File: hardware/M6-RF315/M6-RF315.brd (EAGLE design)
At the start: 90 x 56 mm, 42 parts, among them J1 CON-71439-2164, J2 CON-SMA-VERT, M1 MOUNT-HOLE3.3, M2 MOUNT-HOLE3.3, M3 MOUNT-HOLE3.3, M4 MOUNT-HOLE3.3, M5 FIDUCIAL1X2, M6 FIDUCIAL1X2, M7 FIDUCIAL1X2, M8 FIDUCIAL1X2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

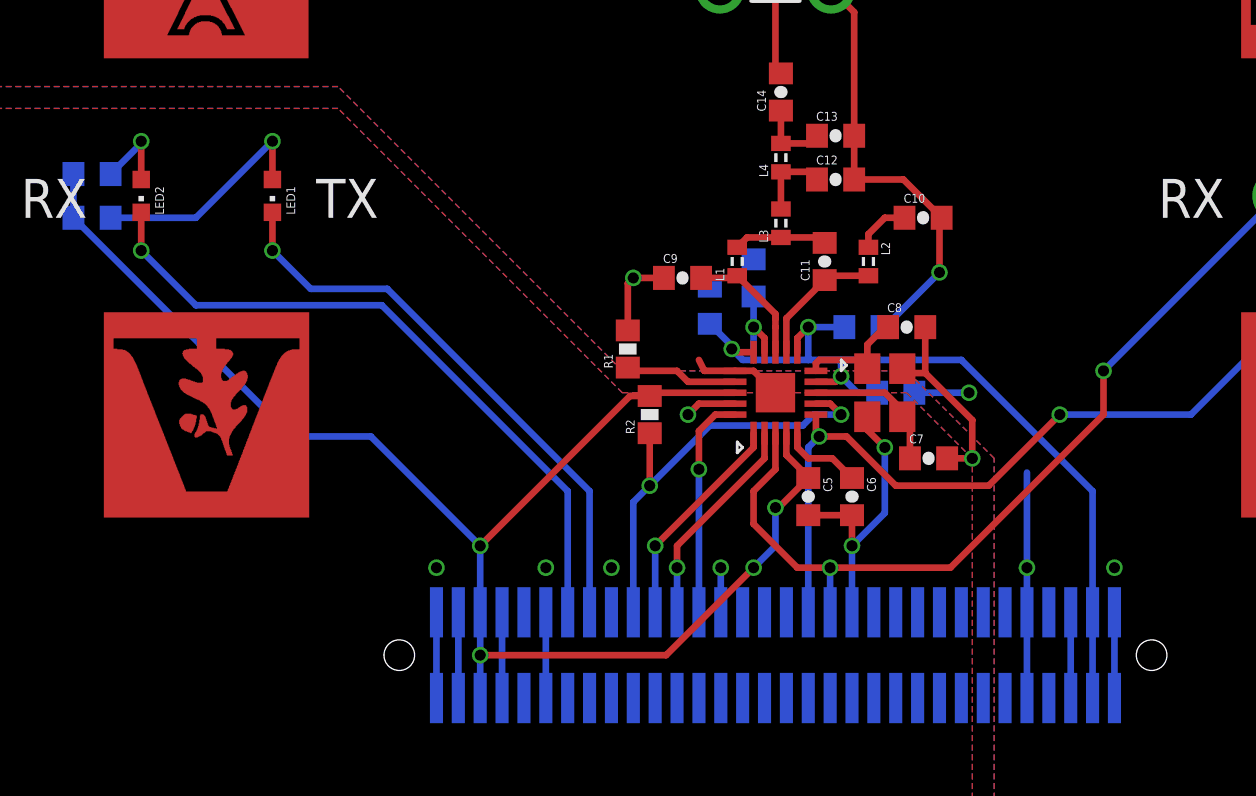
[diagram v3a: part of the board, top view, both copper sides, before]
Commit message: Updated BOM and removed some DRC errors.
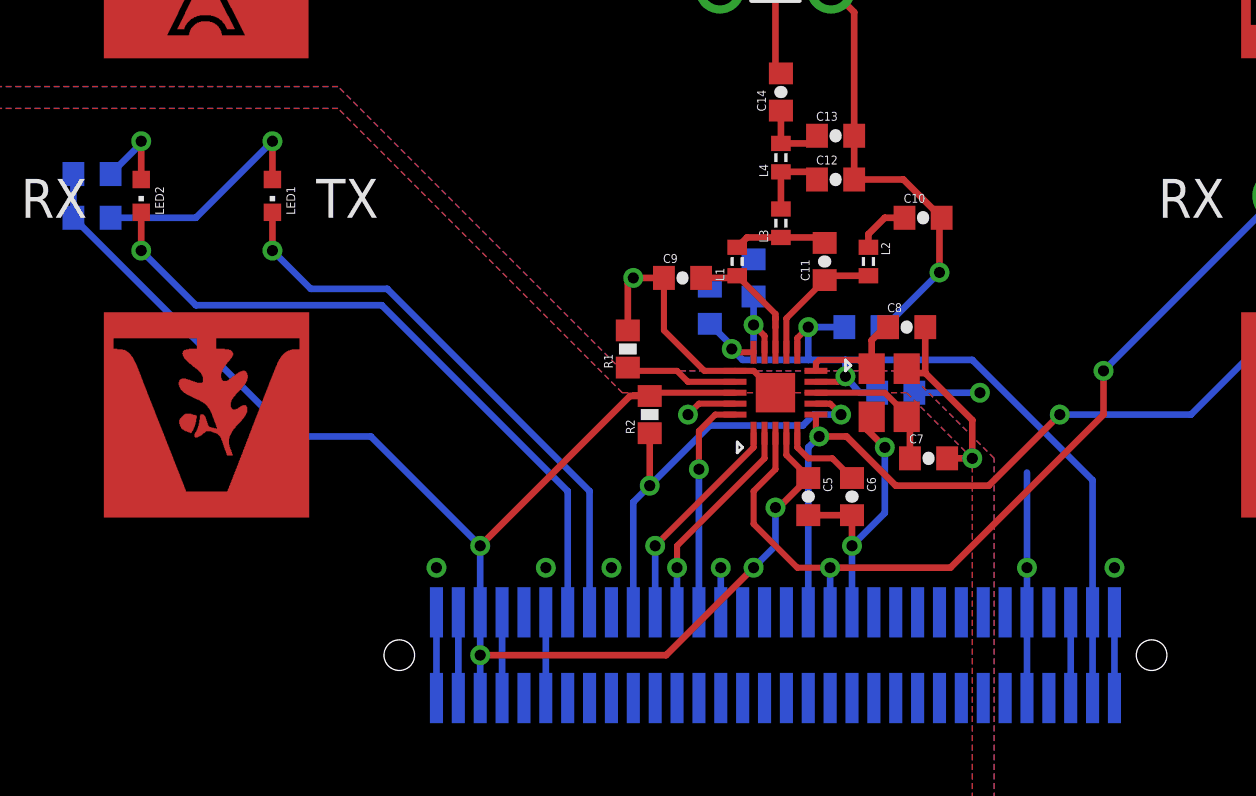
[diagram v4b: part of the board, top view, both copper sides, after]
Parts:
- moved X1 0.20 mm to (50.2, 19.0)
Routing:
- net AGND: track 60.5 -> 65.5 mm

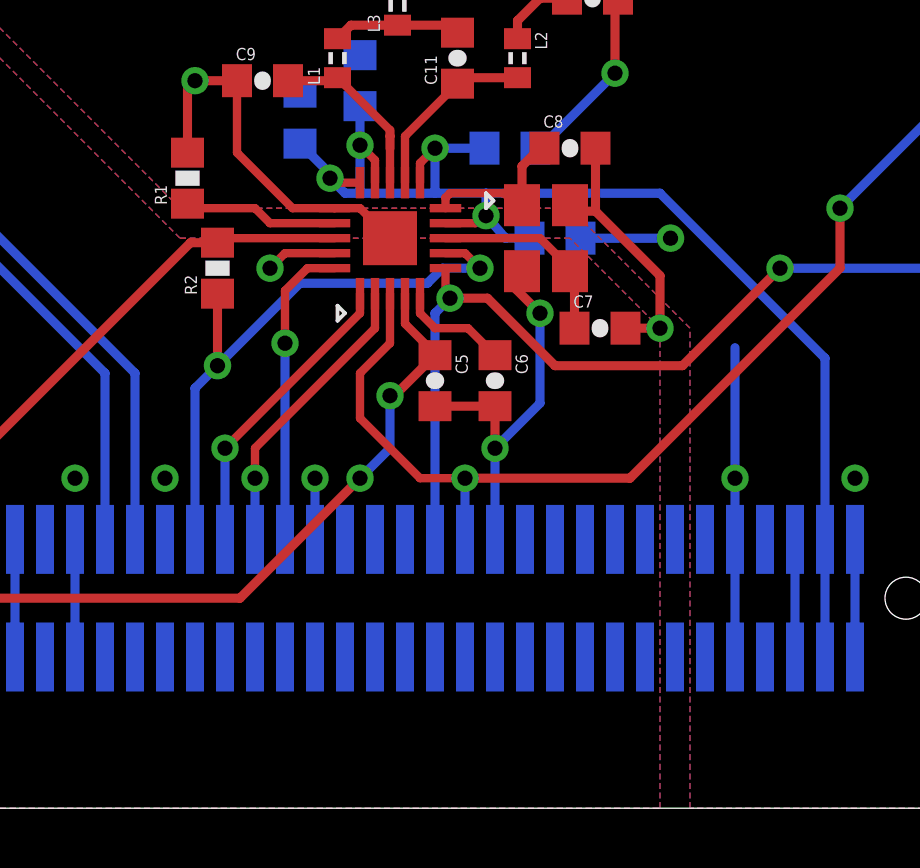
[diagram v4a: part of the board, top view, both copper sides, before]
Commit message: Reviewed DRC errors.
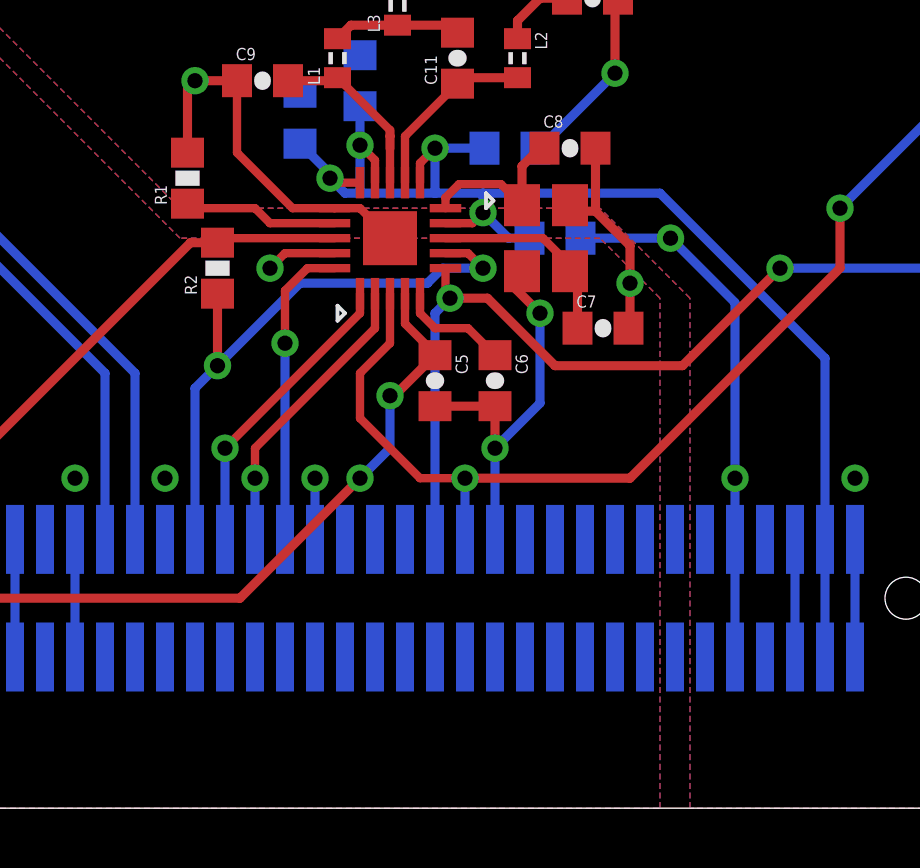
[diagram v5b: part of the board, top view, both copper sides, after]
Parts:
- moved C7 0.10 mm to (52.1, 16.0)
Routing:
- net AGND: track 65.5 -> 70.0 mm
- net DGND: track 34.7 -> 33.1 mm
- net N$7: track 6.94 -> 7.45 mm
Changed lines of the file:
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@@
 <setting verticaltext="up"/>
 </settings>
-<grid distance="1" unitdist="mm" unit="mm" style="lines" multiple="1" display="yes" altdistance="0.1" altunitdist="mm" altunit="mm"/>
+<grid distance="1" unitdist="mm" unit="mm" style="lines" multiple="1" display="yes" altdistance="0.5" altunitdist="mm" altunit="mm"/>
 <layers>
 <layer number="1" name="Top" color="4" fill="1" visible="yes" active="yes"/>
@@
 </element>
 <element name="C6" library="M6-RF315" package="C0603" value="100nF" x="48.5" y="14.25" rot="R270"/>
-<element name="C7" library="M6-RF315" package="C0603" value="12pF" x="52" y="16"/>
+<element name="C7" library="M6-RF315" package="C0603" value="12pF" x="52.1" y="16"/>
 <element name="C8" library="M6-RF315" package="C0603" value="15pF" x="51" y="22"/>
 <element name="TP1" library="M6-RF315" package="TESTPOINT" value="TESTPOINT-RED" x="74" y="28">
@@
 <vertex x="0" y="0"/>
 <vertex x="54" y="0"/>
-<vertex x="54" y="16"/>
-<vertex x="51" y="19"/>
+<vertex x="54" y="17"/>
+<vertex x="52" y="19"/>
 <vertex x="38" y="19"/>
 <vertex x="25" y="32"/>
@@
 <vertex x="0" y="0"/>
 <vertex x="54" y="0"/>
-<vertex x="54" y="16"/>
-<vertex x="51" y="19"/>
+<vertex x="54" y="17"/>
+<vertex x="52" y="19"/>
 <vertex x="38" y="19"/>
 <vertex x="25" y="32"/>
@@
 <wire x1="49.4" y1="17.9" x2="49.2" y2="17.3" width="0.3048" layer="1"/>
 <wire x1="49.2" y1="17.3" x2="50" y2="16.5" width="0.3048" layer="1"/>
-<via x="54" y="16" extent="1-16" drill="0.508"/>
-<wire x1="52.85" y1="16" x2="54" y2="16" width="0.3048" layer="1"/>
+<via x="53" y="17.5" extent="1-16" drill="0.508"/>
 <wire x1="51.85" y1="22" x2="51.85" y2="19.9" width="0.3048" layer="1"/>
-<wire x1="51.85" y1="19.9" x2="54" y2="17.75" width="0.3048" layer="1"/>
-<wire x1="54" y1="17.75" x2="54" y2="16" width="0.3048" layer="1"/>
+<wire x1="51.85" y1="19.9" x2="53" y2="18.75" width="0.3048" layer="1"/>
 <wire x1="51" y1="20.1" x2="51" y2="19.9" width="0.3048" layer="1"/>
 <wire x1="51" y1="19.9" x2="51.85" y2="19.9" width="0.3048" layer="1"/>
@@
 <wire x1="42.5" y1="8.96" x2="42.5" y2="11" width="0.3048" layer="16"/>
 <wire x1="41.5" y1="18.5" x2="41" y2="18" width="0.2794" layer="1"/>
+<wire x1="53" y1="18.75" x2="53" y2="17.5" width="0.3048" layer="1"/>
+<wire x1="53" y1="17.5" x2="53" y2="16.05" width="0.3048" layer="1"/>
+<wire x1="53" y1="16.05" x2="52.95" y2="16" width="0.3048" layer="1"/>
 </signal>
 <signal name="VSUP">
@@
 <wire x1="46" y1="21.5" x2="46.5" y2="22" width="0.2794" layer="1"/>
 <via x="46.5" y="22" extent="1-16" drill="0.508"/>
-<wire x1="46.85" y1="19.5" x2="47.85" y2="19.5" width="0.2794" layer="1"/>
-<wire x1="47.85" y1="19.5" x2="48.2" y2="19.75" width="0.2794" layer="1"/>
-<via x="48.2" y="19.75" extent="1-16" drill="0.508"/>
+<wire x1="46.85" y1="19.5" x2="47.75" y2="19.5" width="0.2794" layer="1"/>
+<wire x1="47.75" y1="19.5" x2="48.1" y2="19.85" width="0.2794" layer="1"/>
+<via x="48.1" y="19.85" extent="1-16" drill="0.508"/>
 <wire x1="44.5" y1="20.85" x2="44.5" y2="21.6" width="0.2794" layer="1"/>
 <via x="44" y="22.1" extent="1-16" drill="0.508"/>
@@
 <wire x1="59.5" y1="8.96" x2="59.5" y2="15" width="0.3048" layer="16"/>
 <wire x1="59.5" y1="15" x2="54" y2="20.5" width="0.3048" layer="16"/>
-<wire x1="54" y1="20.5" x2="48.2" y2="20.5" width="0.3048" layer="16"/>
-<wire x1="48.2" y1="20.5" x2="46.5" y2="20.5" width="0.3048" layer="16"/>
+<wire x1="54" y1="20.5" x2="48.1" y2="20.5" width="0.3048" layer="16"/>
+<wire x1="48.1" y1="20.5" x2="46.5" y2="20.5" width="0.3048" layer="16"/>
 <wire x1="46.5" y1="22" x2="46.5" y2="20.5" width="0.3048" layer="16"/>
-<wire x1="48.2" y1="19.75" x2="48.2" y2="20.5" width="0.3048" layer="16"/>
+<wire x1="48.1" y1="19.85" x2="48.1" y2="20.5" width="0.3048" layer="16"/>
 <via x="43" y="21" extent="1-16" drill="0.508"/>
 <wire x1="42" y1="22.15" x2="43" y2="21.15" width="0.3048" layer="16"/>
@@
 <wire x1="43.5" y1="20.5" x2="44" y2="20.5" width="0.3048" layer="16"/>
 <wire x1="44" y1="20.5" x2="46.5" y2="20.5" width="0.3048" layer="16"/>
-<wire x1="49.65" y1="19" x2="48.85" y2="19" width="0.3048" layer="16"/>
-<wire x1="48.85" y1="19" x2="48.2" y2="19.75" width="0.3048" layer="16"/>
+<wire x1="49.65" y1="19" x2="48.95" y2="19" width="0.3048" layer="16"/>
+<wire x1="48.95" y1="19" x2="48.1" y2="19.85" width="0.3048" layer="16"/>
 <wire x1="46.5" y1="22" x2="48.15" y2="22" width="0.3048" layer="16"/>
 <wire x1="44" y1="20.85" x2="43.15" y2="20.85" width="0.2794" layer="1"/>
@@
 <contactref element="U1" pad="7"/>
 <contactref element="R2" pad="1"/>
-<wire x1="46.85" y1="18.5" x2="47.5" y2="18.5" width="0.2794" layer="1"/>
-<wire x1="47.5" y1="18.5" x2="48" y2="18" width="0.2794" layer="1"/>
-<via x="48" y="18" extent="1-16" drill="0.508"/>
-<wire x1="48" y1="18" x2="46.75" y2="18" width="0.3048" layer="16"/>
+<wire x1="46.85" y1="18.5" x2="47.6" y2="18.5" width="0.2794" layer="1"/>
+<wire x1="47.6" y1="18.5" x2="48.1" y2="18" width="0.2794" layer="1"/>
+<via x="48.1" y="18" extent="1-16" drill="0.508"/>
+<wire x1="48.1" y1="18" x2="46.75" y2="18" width="0.3048" layer="16"/>
 <wire x1="46.75" y1="18" x2="46.25" y2="17.5" width="0.3048" layer="16"/>
 <wire x1="46.25" y1="17.5" x2="42" y2="17.5" width="0.3048" layer="16"/>
@@
 <vertex x="90" y="0"/>
 <vertex x="55" y="0"/>
-<vertex x="55" y="16"/>
-<vertex x="51" y="20"/>
+<vertex x="55" y="17"/>
+<vertex x="52" y="20"/>
 <vertex x="38" y="20"/>
 <vertex x="25" y="33"/>
@@
 <vertex x="90" y="0"/>
 <vertex x="55" y="0"/>
-<vertex x="55" y="16"/>
-<vertex x="51" y="20"/>
+<vertex x="55" y="17"/>
+<vertex x="52" y="20"/>
 <vertex x="38" y="20"/>
 <vertex x="25" y="33"/>
@@
 <wire x1="60.5" y1="8.96" x2="60.5" y2="5.04" width="0.3048" layer="16"/>
 <wire x1="56.5" y1="8.96" x2="56.5" y2="11" width="0.3048" layer="16"/>
-<wire x1="56.5" y1="11" x2="56.5" y2="15.35" width="0.3048" layer="16"/>
+<wire x1="56.5" y1="11" x2="56.5" y2="16.85" width="0.3048" layer="16"/>
 <via x="38.5" y="24.25" extent="1-16" drill="0.508"/>
 <wire x1="43.15" y1="20" x2="41.75" y2="20" width="0.2794" layer="1"/>
@@
 <wire x1="41.75" y1="20" x2="39.9" y2="21.85" width="0.2794" layer="1"/>
 <wire x1="39.9" y1="21.85" x2="39.9" y2="24.25" width="0.2794" layer="1"/>
-<wire x1="60.5" y1="8.96" x2="60.5" y2="11" width="0" layer="19" extent="16-16"/>
-<wire x1="56.5" y1="11" x2="60.5" y2="11" width="0" layer="19" extent="16-16"/>
-<wire x1="54.35" y1="19" x2="56.5" y2="15.35" width="0" layer="19" extent="16-16"/>
-<wire x1="50" y1="22" x2="51" y2="19" width="0" layer="19" extent="16-16"/>
-<wire x1="45" y1="19" x2="49.85" y2="22" width="0" layer="19" extent="1-16"/>
-<wire x1="42" y1="23.85" x2="39.9" y2="24.25" width="0" layer="19" extent="1-16"/>
-<wire x1="44" y1="25.1" x2="42" y2="23.85" width="0" layer="19" extent="16-16"/>
+<wire x1="56.5" y1="16.85" x2="54.35" y2="19" width="0.3048" layer="16"/>
 </signal>
 <signal name="PB4">
@@
 <wire x1="49.4" y1="20.1" x2="49.4" y2="21.4" width="0.3048" layer="1"/>
 <wire x1="46.85" y1="20" x2="46.85" y2="20.35" width="0.2794" layer="1"/>
-<wire x1="46.85" y1="20.35" x2="47" y2="20.5" width="0.2794" layer="1"/>
-<wire x1="47" y1="20.5" x2="48.8" y2="20.5" width="0.2794" layer="1"/>
-<wire x1="48.8" y1="20.5" x2="49.4" y2="20.1" width="0.3048" layer="1"/>
+<wire x1="46.85" y1="20.35" x2="47.3" y2="20.8" width="0.2794" layer="1"/>
+<wire x1="47.3" y1="20.8" x2="48.7" y2="20.8" width="0.2794" layer="1"/>
+<wire x1="48.7" y1="20.8" x2="49.4" y2="20.1" width="0.2794" layer="1"/>
 <wire x1="49.4" y1="21.4" x2="50" y2="22" width="0.3048" layer="1"/>
 <wire x1="50" y1="22" x2="50.15" y2="22" width="0.3048" layer="1"/>
@@
 <contactref element="C7" pad="1"/>
 <contactref element="X1" pad="3"/>
-<wire x1="46.85" y1="19" x2="50" y2="19" width="0.2794" layer="1"/>
+<wire x1="46.85" y1="19" x2="50.1" y2="19" width="0.2794" layer="1"/>
 <wire x1="51" y1="18" x2="50.9" y2="18" width="0.3048" layer="1"/>
 <wire x1="50.9" y1="18" x2="51" y2="17.9" width="0.3048" layer="1"/>
 <wire x1="51" y1="17.9" x2="51" y2="17.7" width="0.3048" layer="1"/>
-<wire x1="51.15" y1="16" x2="51.15" y2="17.55" width="0.3048" layer="1"/>
 <wire x1="51.15" y1="17.55" x2="51" y2="17.9" width="0.3048" layer="1"/>
-<wire x1="50" y1="19" x2="51" y2="18" width="0.2794" layer="1"/>
+<wire x1="50.1" y1="19" x2="51" y2="18.1" width="0.2794" layer="1"/>
+<wire x1="51" y1="18.1" x2="51" y2="18" width="0.2794" layer="1"/>
+<wire x1="51.25" y1="16" x2="51.25" y2="17.65" width="0.3048" layer="1"/>
+<wire x1="51.25" y1="17.65" x2="51" y2="17.9" width="0.3048" layer="1"/>
 </signal>
 <signal name="N$8">

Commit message: Added exported GERBER files.
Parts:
- LOGO4: value LOGO-RADIO-2-600MIL-10MM-CU -> LOGO-RADIO-3-600MIL-10MM-CU; device M6-RF315:LOGO-RADIO-2-10MM-COPPER -> M6-RF315:LOGO-RADIO-FILLED-10MM-COPPER
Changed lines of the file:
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@@
 <attribute name="FUNCTION" value="RF LC filter/matching filter inductor" x="45.25" y="29.75" size="1.778" layer="27" rot="R90" display="off"/>
 </element>
-<element name="LOGO4" library="M6-RF315" package="LOGO-RADIO-2-10MM-COPPER" value="LOGO-RADIO-2-600MIL-10MM-CU" x="14" y="34"/>
+<element name="LOGO4" library="M6-RF315" package="LOGO-RADIO-FILLED-10MM-COPPER" value="LOGO-RADIO-3-600MIL-10MM-CU" x="14" y="34"/>
 <element name="X1" library="M6-RF315" package="NX3225GA" value="NX3225GA" x="50.2" y="19" rot="R270">
 <attribute name="MFN" value="NX3225GA-16.000M-STD-CRG-1" x="50.2" y="19" size="1.778" layer="27" rot="R270" display="off"/>
